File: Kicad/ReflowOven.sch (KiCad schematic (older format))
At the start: 19 parts, among them J1 Relay_Conn, P1 USB_B, SW1 Reset, SW2 TEST_SW, U1 AD595AQ, U2 AT90USB646-MU, Y1 16Mhz

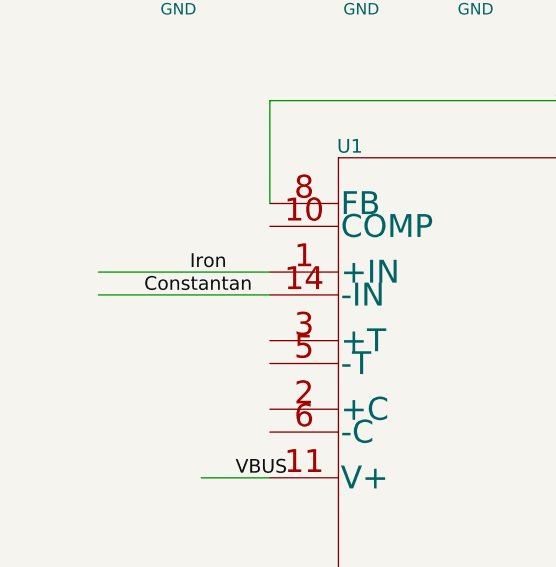
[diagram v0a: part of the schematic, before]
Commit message: Added pads for TCOUPLE
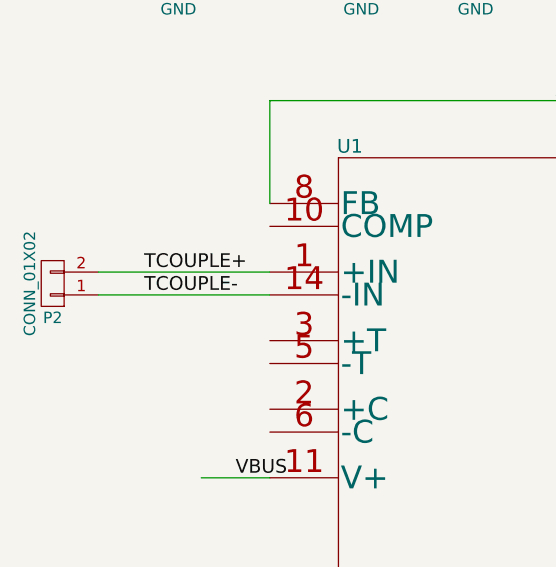
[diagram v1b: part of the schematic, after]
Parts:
- added P2: CONN_01X02, symbol CONN_01X02
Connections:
- net labels added: TCOUPLE+, TCOUPLE-
- net labels removed: Constantan, Iron
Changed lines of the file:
@@
 	-1   0    0    1
 $EndComp
-Text Label 1350 5050 0    60   ~ 0
-Iron
+Text Label 1150 5050 0    60   ~ 0
+TCOUPLE+
 Text Label 1150 5150 0    60   ~ 0
-Constantan
+TCOUPLE-
 Text Label 2950 4300 0    60   ~ 0
 Analog_out
@@
 	0    -1   -1   0
 $EndComp
+$Comp
+L CONN_01X02 P2
+U 1 1 59555CE0
+P 750 5100
+F 0 "P2" H 750 5250 50  0000 C CNN
+F 1 "CONN_01X02" V 850 5100 50  0000 C CNN
+F 2 "" H 750 5100 50  0001 C CNN
+F 3 "" H 750 5100 50  0000 C CNN
+	1    750  5100
+	-1   0    0    1
+$EndComp
 $EndSCHEMATC

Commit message: Update
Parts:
- removed P1: USB_B, Connectors:USB_B, symbol USB_B
- removed P2: CONN_01X02, symbol CONN_01X02
- added C6: 0.1uf, Capacitors_SMD:C_0805_HandSoldering, symbol C
- added GS1: GS2, Connectors:GS2, symbol GS2
- added GS3: GS4, Connectors:GS2, symbol GS2
- added P1: USB_OTG, fmcw2_mcu:USB_MICRO, symbol USB_OTG
- added P2: HE10-10, Connectors:he10-10d, symbol HE10-10
- added Q1: BC817-40, TO_SOT_Packages_SMD:SOT-23, symbol BC817-40
- added R4, R5, R6, R7, R8: 1k, Resistors_SMD:R_0805_HandSoldering, symbol R
- C2, C3: value 22pf -> 10pf
- R1: value 1M -> 1k
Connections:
- net labels added: HWB, Relay
- net labels removed: Relay+, Relay-
- wire segments 66 -> 114
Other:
- moved on the sheet: C1, D3, D4, D5, J1, U1

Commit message: Modified Files
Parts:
- removed C3: 10pf, Capacitors_SMD:C_0805_HandSoldering, symbol C
- removed C6: 0.1uf, Capacitors_SMD:C_0805_HandSoldering, symbol C
- removed Y1: 16Mhz, Crystals:Crystal_AT310_d3.0mm_l10.0mm_Horizontal, symbol Crystal
- added R10: 24k, Resistors_SMD:R_0805_HandSoldering, symbol R
- added R9: 12k, Resistors_SMD:R_0805_HandSoldering, symbol R
- added Y1: 16Mhz, Crystals:Crystal_SMD_3225-4pin_3.2x2.5mm_HandSoldering, symbol Crystal_GND24
- C1: value 2.2uf -> 10uf
- C2: value 10pf -> 0.01uf
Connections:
- net labels added: VBUS_3V3
- wire segments 114 -> 118
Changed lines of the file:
@@
 LIBS:switches
 LIBS:AT90USB646-MU
+LIBS:ReflowOven-cache
 EELAYER 25 0
 EELAYER END
@@
 P 2000 1350
 F 0 "C1" H 2025 1450 50  0000 L CNN
-F 1 "2.2uf" H 2025 1250 50  0000 L CNN
+F 1 "10uf" H 2025 1250 50  0000 L CNN
 F 2 "Capacitors_SMD:C_0805_HandSoldering" H 2038 1200 50  0001 C CNN
 F 3 "" H 2000 1350 50  0000 C CNN
@@
 	1    4750 7400
 	1    0    0    -1
-$EndComp
-$Comp
-L Crystal Y1
-U 1 1 5953A7C8
-P 4750 2250
-F 0 "Y1" H 4750 2400 50  0000 C CNN
-F 1 "16Mhz" V 4950 2250 50  0000 C CNN
-F 2 "Crystals:Crystal_AT310_d3.0mm_l10.0mm_Horizontal" H 4750 2250 50  0001 C CNN
-F 3 "" H 4750 2250 50  0000 C CNN
-	1    4750 2250
-	0    1    1    0
-$EndComp
-$Comp
-L C C2
-U 1 1 5953A88E
-P 4300 2100
-F 0 "C2" H 4325 2200 50  0000 L CNN
-F 1 "10pf" H 4325 2000 50  0000 L CNN
-F 2 "Capacitors_SMD:C_0805_HandSoldering" H 4338 1950 50  0001 C CNN
-F 3 "" H 4300 2100 50  0000 C CNN
-	1    4300 2100
-	0    1    1    0
-$EndComp
-$Comp
-L C C3
-U 1 1 5953A8D1
-P 4300 2400
-F 0 "C3" H 4325 2500 50  0000 L CNN
-F 1 "10pf" H 4250 2300 50  0000 L CNN
-F 2 "Capacitors_SMD:C_0805_HandSoldering" H 4338 2250 50  0001 C CNN
-F 3 "" H 4300 2400 50  0000 C CNN
-	1    4300 2400
-	0    1    1    0
 $EndComp
 Text Label 1300 1450 0    60   ~ 0
@@
 	1    0    0    -1
 $EndComp
-$Comp
-L GND #PWR04
-U 1 1 59546E94
-P 4050 2250
-F 0 "#PWR04" H 4050 2000 50  0001 C CNN
-F 1 "GND" H 4050 2100 50  0000 C CNN
-F 2 "" H 4050 2250 50  0000 C CNN
-F 3 "" H 4050 2250 50  0000 C CNN
-	1    4050 2250
-	0    1    1    0
-$EndComp
 Text Label 5400 2300 0    60   ~ 0
 VBUS
@@
 $EndComp
 $Comp
-L GND #PWR05
+L GND #PWR04
 U 1 1 59547856
 P 4600 4300
-F 0 "#PWR05" H 4600 4050 50  0001 C CNN
+F 0 "#PWR04" H 4600 4050 50  0001 C CNN
 F 1 "GND" H 4600 4150 50  0000 C CNN
 F 2 "" H 4600 4300 50  0000 C CNN
@@
 $EndComp
 $Comp
-L GND #PWR06
+L GND #PWR05
 U 1 1 59547A2C
 P 5350 5900
-F 0 "#PWR06" H 5350 5650 50  0001 C CNN
+F 0 "#PWR05" H 5350 5650 50  0001 C CNN
 F 1 "GND" H 5350 5750 50  0000 C CNN
 F 2 "" H 5350 5900 50  0000 C CNN
@@
 $EndComp
 $Comp
-L GND #PWR07
+L GND #PWR06
 U 1 1 595480C7
 P 5250 700
-F 0 "#PWR07" H 5250 450 50  0001 C CNN
+F 0 "#PWR06" H 5250 450 50  0001 C CNN
 F 1 "GND" H 5250 550 50  0000 C CNN
 F 2 "" H 5250 700 50  0000 C CNN
@@
 $EndComp
 $Comp
-L GND #PWR08
+L GND #PWR07
 U 1 1 59549079
 P 2100 3750
-F 0 "#PWR08" H 2100 3500 50  0001 C CNN
+F 0 "#PWR07" H 2100 3500 50  0001 C CNN
 F 1 "GND" H 2100 3600 50  0000 C CNN
 F 2 "" H 2100 3750 50  0000 C CNN
@@
 $EndComp
 $Comp
-L GND #PWR09
+L GND #PWR08
 U 1 1 59549B5E
 P 2600 3750
-F 0 "#PWR09" H 2600 3500 50  0001 C CNN
+F 0 "#PWR08" H 2600 3500 50  0001 C CNN
 F 1 "GND" H 2600 3600 50  0000 C CNN
 F 2 "" H 2600 3750 50  0000 C CNN
@@
 $EndComp
 $Comp
-L GND #PWR010
+L GND #PWR09
 U 1 1 5954AD9F
 P 3200 3750
-F 0 "#PWR010" H 3200 3500 50  0001 C CNN
+F 0 "#PWR09" H 3200 3500 50  0001 C CNN
 F 1 "GND" H 3200 3600 50  0000 C CNN
 F 2 "" H 3200 3750 50  0000 C CNN
@@
 $EndComp
 $Comp
-L GND #PWR011
+L GND #PWR010
 U 1 1 5954B5CB
 P 3900 3750
-F 0 "#PWR011" H 3900 3500 50  0001 C CNN
+F 0 "#PWR010" H 3900 3500 50  0001 C CNN
 F 1 "GND" H 3900 3600 50  0000 C CNN
 F 2 "" H 3900 3750 50  0000 C CNN
@@
 $EndComp
 $Comp
-L GND #PWR012
+L GND #PWR011
 U 1 1 5954BCA4
 P 1550 3750
-F 0 "#PWR012" H 1550 3500 50  0001 C CNN
+F 0 "#PWR011" H 1550 3500 50  0001 C CNN
 F 1 "GND" H 1550 3600 50  0000 C CNN
 F 2 "" H 1550 3750 50  0000 C CNN
@@
 $EndComp
 $Comp
-L GND #PWR013
+L GND #PWR012
 U 1 1 595518EE
 P 2400 7000
-F 0 "#PWR013" H 2400 6750 50  0001 C CNN
+F 0 "#PWR012" H 2400 6750 50  0001 C CNN
 F 1 "GND" H 2400 6850 50  0000 C CNN
 F 2 "" H 2400 7000 50  0000 C CNN
@@
 	2000 1200 2000 950
 Wire Wire Line
-	4450 2400 5600 2400
-Connection ~ 4750 2100
-Connection ~ 4750 2400
-Wire Wire Line
-	4150 2100 4150 2400
-Wire Wire Line
-	4050 2250 4150 2250
-Connection ~ 4150 2250
-Wire Wire Line
 	1000 1450 1450 1450
 Wire Wire Line
@@
 Wire Wire Line
 	1000 1650 1450 1650
-Wire Wire Line
-	4450 2100 4750 2100
-Wire Wire Line
-	4750 2100 4750 850
-Wire Wire Line
-	4750 850  9600 850
-Wire Wire Line
-	9600 850  9600 1400
 Wire Wire Line
 	5600 2300 5050 2300
@@
 	9600 1500 10100 1500
 Connection ~ 5550 2200
-$Comp
-L C C6
-U 1 1 59565EDD
-P 5300 1700
-F 0 "C6" H 5200 1800 50  0000 L CNN
-F 1 "0.1uf" V 5250 1450 50  0000 L CNN
-F 2 "Capacitors_SMD:C_0805_HandSoldering" H 5338 1550 50  0001 C CNN
-F 3 "" H 5300 1700 50  0000 C CNN
-	1    5300 1700
-	0    1    1    0
-$EndComp
-Wire Wire Line
-	5150 1700 5050 1700
-$Comp
-L GND #PWR014
-U 1 1 59566066
-P 5050 1700
-F 0 "#PWR014" H 5050 1450 50  0001 C CNN
-F 1 "GND" H 5050 1550 50  0000 C CNN
-F 2 "" H 5050 1700 50  0000 C CNN
-F 3 "" H 5050 1700 50  0000 C CNN
-	1    5050 1700
-	0    1    1    0
-$EndComp
-Wire Wire Line
-	5600 1700 5450 1700
 Wire Wire Line
 	5600 1400 5600 1700
@@
 VBUS
 $Comp
-L GND #PWR015
+L GND #PWR013
 U 1 1 59578A93
 P 900 3150
-F 0 "#PWR015" H 900 2900 50  0001 C CNN
+F 0 "#PWR013" H 900 2900 50  0001 C CNN
 F 1 "GND" H 900 3000 50  0000 C CNN
 F 2 "" H 900 3150 50  0000 C CNN
@@
 	5750 6900 5750 6700
 $Comp
-L GND #PWR016
+L GND #PWR014
 U 1 1 595835FA
 P 5750 6700
-F 0 "#PWR016" H 5750 6450 50  0001 C CNN
+F 0 "#PWR014" H 5750 6450 50  0001 C CNN
 F 1 "GND" H 5750 6550 50  0000 C CNN
 F 2 "" H 5750 6700 50  0000 C CNN
@@
 Text Label 6450 7100 0    60   ~ 0
 Relay
+$Comp
+L Crystal_GND24 Y1
+U 1 1 595F8BF3
+P 4750 2250
+F 0 "Y1" V 4600 2350 50  0000 L CNN
+F 1 "16Mhz" V 4950 2150 50  0000 L CNN
+F 2 "Crystals:Crystal_SMD_3225-4pin_3.2x2.5mm_HandSoldering" H 4750 2250 50  0001 C CNN
+F 3 "" H 4750 2250 50  0000 C CNN
+	1    4750 2250
+	0    1    1    0
+$EndComp
+Wire Wire Line
+	4750 2400 5600 2400
+Wire Wire Line
+	4000 2250 4550 2250
+Wire Wire Line
+	4500 2250 4500 2100
+Connection ~ 4500 2250
+Wire Wire Line
+	4500 2100 4750 2100
+$Comp
+L C C2
+U 1 1 5978FFAA
+P 4500 1950
+F 0 "C2" H 4525 2050 50  0000 L CNN
+F 1 "0.01uf" H 4525 1850 50  0000 L CNN
+F 2 "Capacitors_SMD:C_0805_HandSoldering" H 4538 1800 50  0001 C CNN
+F 3 "" H 4500 1950 50  0000 C CNN
+	1    4500 1950
+	0    1    1    0
+$EndComp
+Wire Wire Line
+	4950 2250 4950 2050
+Wire Wire Line
+	4950 2050 4650 2050
+Wire Wire Line
+	4650 2050 4650 1950
+$Comp
+L GND #PWR015
+U 1 1 59792BA2
+P 5000 2200
+F 0 "#PWR015" H 5000 1950 50  0001 C CNN
+F 1 "GND" H 5000 2050 50  0000 C CNN
+F 2 "" H 5000 2200 50  0000 C CNN
+F 3 "" H 5000 2200 50  0000 C CNN
+	1    5000 2200
+	0    -1   -1   0
+$EndComp
+Wire Wire Line
+	5000 2200 4950 2200
+Connection ~ 4950 2200
+$Comp
+L R R9
+U 1 1 59793D17
+P 3250 1200
+F 0 "R9" V 3330 1200 50  0000 C CNN
+F 1 "12k" V 3250 1200 50  0000 C CNN
+F 2 "Resistors_SMD:R_0805_HandSoldering" V 3180 1200 50  0001 C CNN
+F 3 "" H 3250 1200 50  0000 C CNN
+	1    3250 1200
+	1    0    0    -1
+$EndComp
+$Comp
+L R R10
+U 1 1 59793D8C
+P 3250 1600
+F 0 "R10" V 3330 1600 50  0000 C CNN
+F 1 "24k" V 3250 1600 50  0000 C CNN
+F 2 "Resistors_SMD:R_0805_HandSoldering" V 3180 1600 50  0001 C CNN
+F 3 "" H 3250 1600 50  0000 C CNN
+	1    3250 1600
+	1    0    0    -1
+$EndComp
+$Comp
+L GND #PWR016
+U 1 1 59793DEF
+P 3250 1850
+F 0 "#PWR016" H 3250 1600 50  0001 C CNN
+F 1 "GND" H 3250 1700 50  0000 C CNN
+F 2 "" H 3250 1850 50  0000 C CNN
+F 3 "" H 3250 1850 50  0000 C CNN
+	1    3250 1850
+	1    0    0    -1
+$EndComp
+Wire Wire Line
+	3250 1850 3250 1750
+Wire Wire Line
+	3250 1450 3250 1350
+Wire Wire Line
+	3250 1050 3250 800
+Text Label 3250 900  0    60   ~ 0
+VBUS
+Wire Wire Line
+	3250 1400 3600 1400
+Connection ~ 3250 1400
+Text Label 3400 1400 0    60   ~ 0
+VBUS_3V3
+Text Label 4000 2250 0    60   ~ 0
+VBUS_3V3
+Wire Wire Line
+	4350 1950 4000 1950
+Text Label 4000 1950 0    60   ~ 0
+VBUS_3V3
 $EndSCHEMATC
